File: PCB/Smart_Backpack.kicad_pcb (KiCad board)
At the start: 2 copper layers, 65.8 x 74.4 mm, 57 parts, among them J1 Conn_01x03_Pin, J2 Conn_01x02_Pin, J3 Conn_01x02_Pin, J4 Conn_01x03_Pin, J5 Conn_01x03_Pin, J6 Conn_01x03_Pin, J7 Conn_01x07_Pin, J8 Conn_01x08_Socket, J9 USB_C_Receptacle_USB2.0_16P, SW1 SW_Push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

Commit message: PCB revision 1 is finished!!!!
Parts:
- moved D2 4.09 mm to (93.2, 84.8), turned to 90 degrees
- moved R20 2.39 mm to (95.5, 85.6)
- moved R12 2.09 mm to (97.8, 87.4)
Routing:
- net +3V3: track 39.9 -> 241.8 mm, vias 1 -> 5
- net GND: track 0.00 -> 48.8 mm, vias 0 -> 7
- net Net-(C9-Pad1): track 5.62 -> 12.1 mm
- net Net-(C11-Pad1): track 4.91 -> 10.7 mm
- net unconnected-(U3-IO4-Pad24): track 0.00 -> 2.45 mm, vias 0 -> 1
- net Net-(J9-CC1): track 5.25 -> 7.40 mm
- net unconnected-(U3-IO19-Pad33): track 0.00 -> 2.09 mm, vias 0 -> 1
- net unconnected-(U3-IO21-Pad35): track 0.00 -> 2.04 mm, vias 0 -> 1
- net unconnected-(U3-IO5-Pad29): track 0.00 -> 1.78 mm, vias 0 -> 1
- net Flash_TXD: track 37.9 -> 39.5 mm, vias 0 -> 1
- net IMU_SDA: track 42.4 -> 41.0 mm
- net Flash_RXD: track 37.3 -> 38.6 mm, vias 0 -> 1
- net Net-(D2-A): track 3.28 -> 2.32 mm
- net FLEX_1: track 64.7 -> 64.6 mm, vias 0 -> 1
- added copper zone on B.Cu, net GND
- added copper zone on F.Cu, net GND
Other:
- outline, holes or cut-outs redrawn
- board text added: "Flash RX"
- board text added: "FlashTX"
- board text added: "IO19"
- board text added: "IO21"
- board text added: "IO4"
- board text added: "IO5"

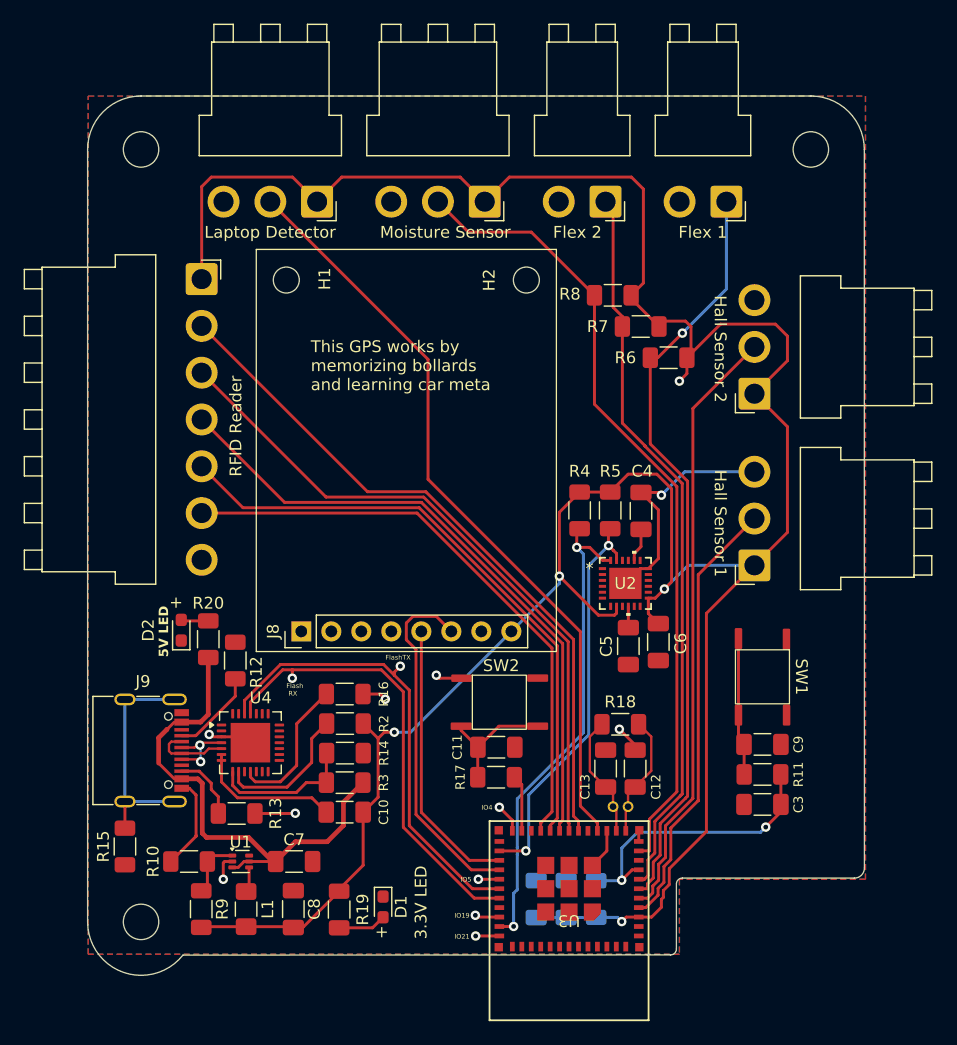
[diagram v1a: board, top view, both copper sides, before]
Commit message: add ground vias, RTC protection, and mounting hole exclusion zones
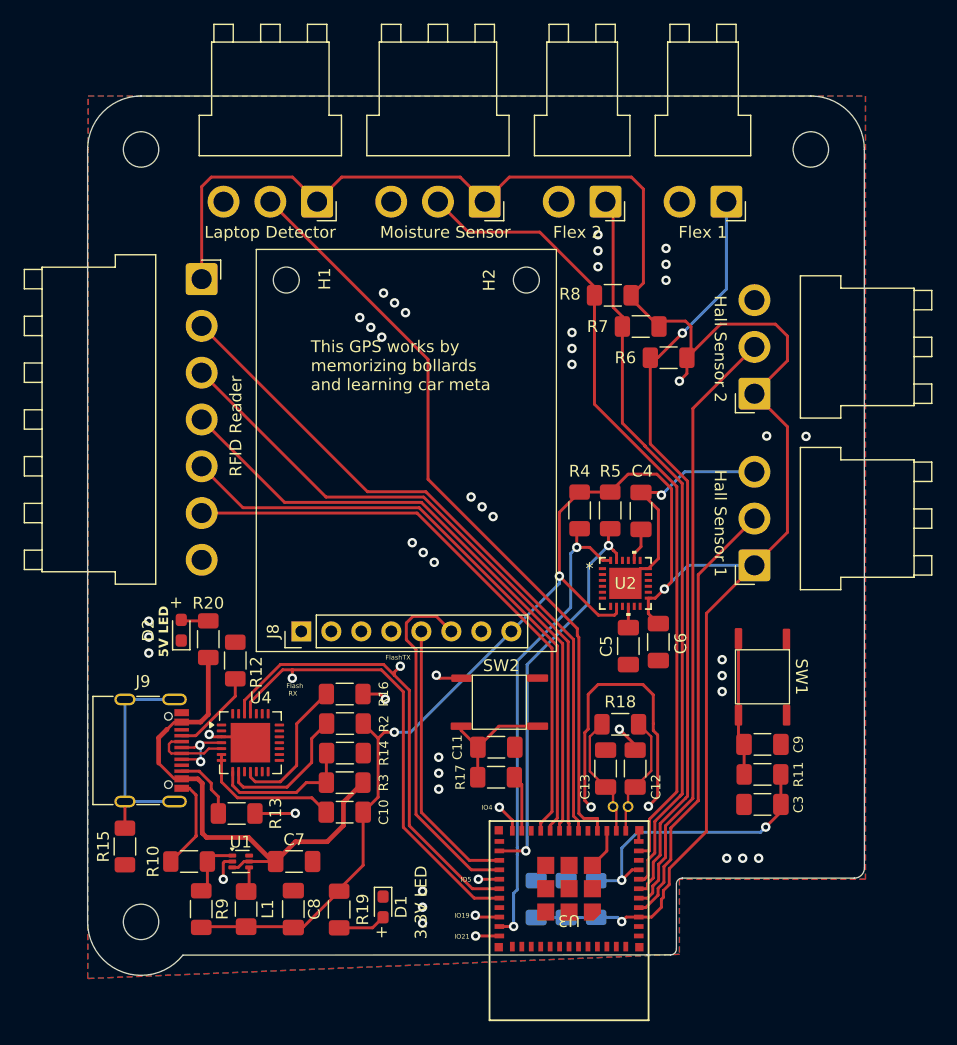
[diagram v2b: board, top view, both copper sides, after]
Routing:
- net GND: track 48.8 -> 74.9 mm, vias 7 -> 47
- net LAPTOP: track 64.7 -> 65.4 mm

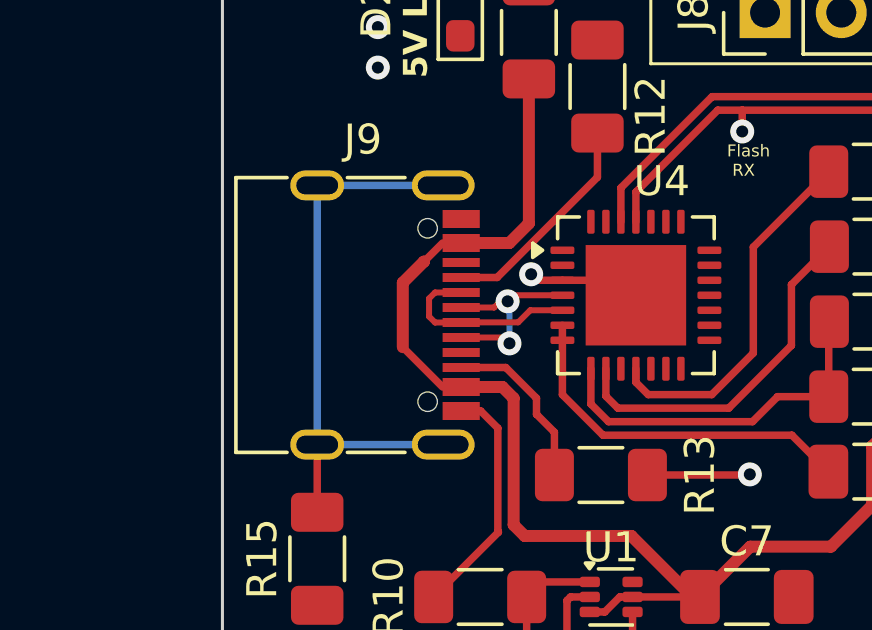
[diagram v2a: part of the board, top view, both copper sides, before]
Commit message: Some updates suggested by Ryan (The 1 sem senior design prof)
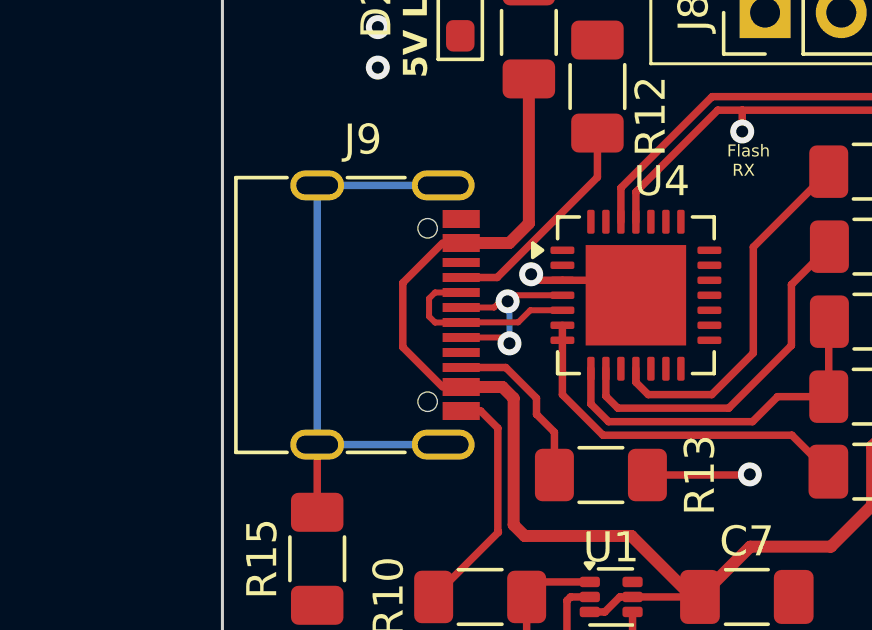
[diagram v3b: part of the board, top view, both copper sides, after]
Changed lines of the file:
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@@
-	)
-	(segment
-		(start 91.302 96.09)
-		(end 91.302 93.94)
-		(width 0.4)
-		(layer "F.Cu")
-		(net 21)
 	)
 	(segment
 		(start 100.954 104.415)
 		(end 98.922 102.383)
-		(width 0.4)
-		(layer "F.Cu")
-		(net 21)
-	)
-	(segment
-		(start 92.005 93.237)
-		(end 92.010364 93.237)
 		(width 0.4)
 		(layer "F.Cu")
@@
 	)
 	(segment
-		(start 92.629 97.417)
-		(end 91.302 96.09)
-		(width 0.25)
-		(layer "F.Cu")
-		(net 21)
-	)
-	(segment
 		(start 94.853124 92.617)
 		(end 95.504 91.966124)
@@
 	)
 	(segment
-		(start 91.302 93.94)
-		(end 92.005 93.237)
-		(width 0.4)
-		(layer "F.Cu")
-		(net 21)
-	)
-	(segment
 		(start 97.5355 104.915)
 		(end 98.035798 104.915)
-		(width 0.25)
-		(layer "F.Cu")
-		(net 21)
-	)
-	(segment
-		(start 92.010364 93.237)
-		(end 92.630364 92.617)
 		(width 0.25)
 		(layer "F.Cu")
@@
 	)
 	(segment
+		(start 92.630364 92.617)
+		(end 91.302 93.945364)
+		(width 0.25)
+		(layer "F.Cu")
+		(net 21)
+	)
+	(segment
 		(start 95.504 91.966124)
 		(end 95.504 87.148)
@@
 		(end 94.996 97.79)
 		(width 0.4)
+		(layer "F.Cu")
+		(net 21)
+	)
+	(segment
+		(start 91.302 93.945364)
+		(end 91.302 96.09)
+		(width 0.25)
 		(layer "F.Cu")
 		(net 21)
@@
 		(layer "F.Cu")
 		(net 21)
+	)
+	(segment
+		(start 91.302 96.09)
+		(end 92.629 97.417)
+		(width 0.25)
+		(layer "F.Cu")
+		(net 21)

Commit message: Literally just added our names
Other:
- board text added: "ECE49595 Team 10 Colin Fennen Grant Sylvester Josie Thomas Jack Douthit"
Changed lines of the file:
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@@
 		(layer "Edge.Cuts")
+	)
+	(gr_text "ECE49595\nTeam 10\nColin Fennen\nGrant Sylvester\nJosie Thomas\nJack Douthit"
+		(at 149.098 104.14 0)
+		(layer "B.Cu")
+		(effects
+			(font
+				(size 1.016 1.016)
+				(thickness 0.2286)
+				(bold yes)
+			)
+			(justify left bottom mirror)
+		)
 	)
 	(gr_text "+"

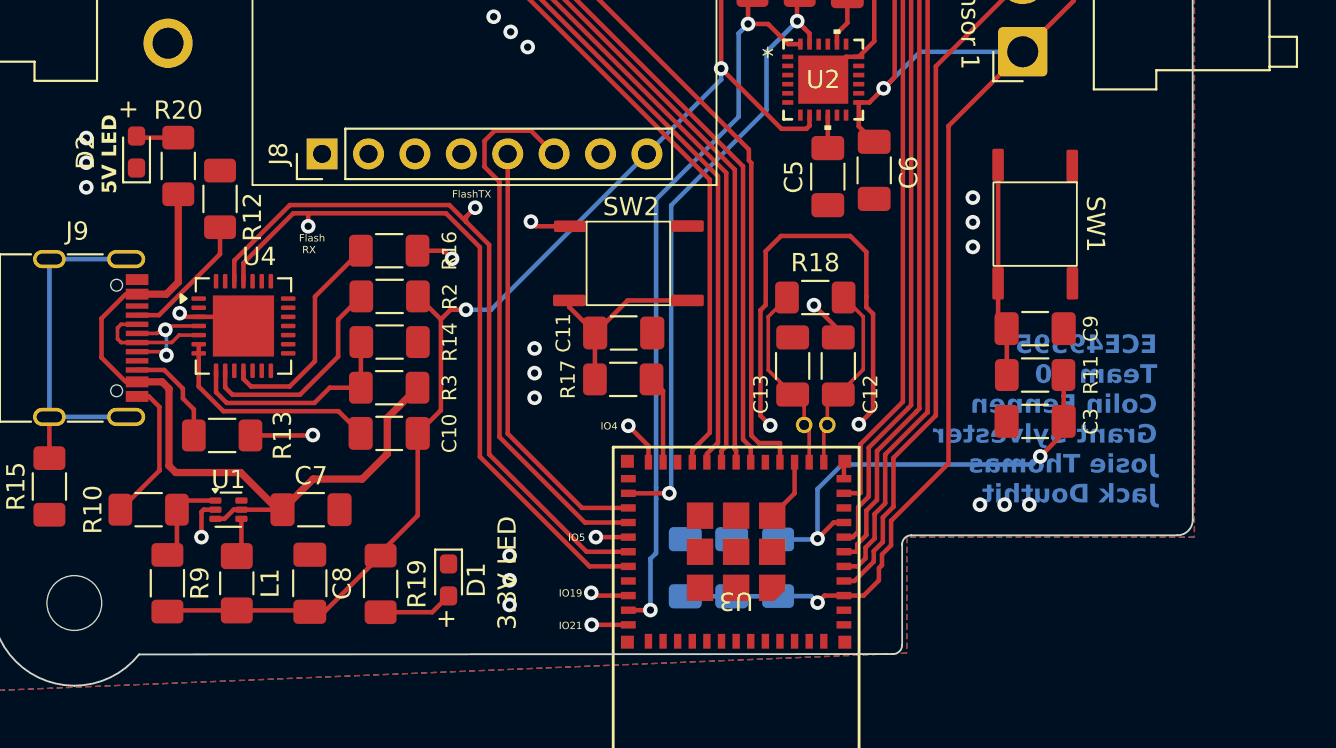
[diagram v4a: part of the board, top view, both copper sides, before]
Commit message: Added motors :pensive:
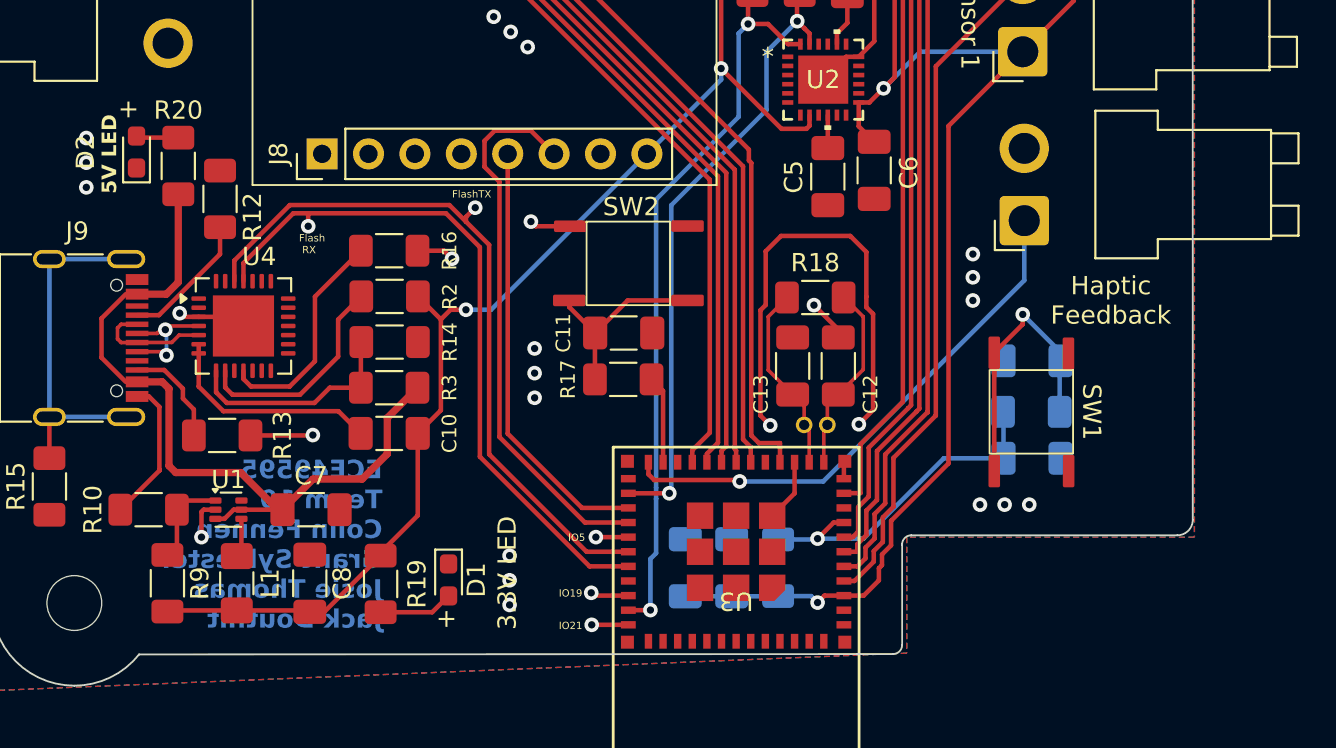
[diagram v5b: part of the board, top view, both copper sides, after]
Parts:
- added Haptic Feedback: Conn_01x02_Pin, Connector_JST:JST_VH_B2PS-VH_1x02_P3.96mm_Horizontal, F.Cu at (141.8, 88.6)
- C3, C9, R11: moved to B.Cu
- moved SW1 10.3 mm to (142.2, 99.1)
- moved R11 2.03 mm to (142.2, 99.1), turned to 180 degrees
- moved C3 2.02 mm to (142.2, 101.6), turned to 0 degrees
- moved C9 1.77 mm to (142.2, 96.3), turned to 180 degrees
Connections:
- U3 pad 24: unconnected-(U3-IO4-Pad24) -> MOTOR
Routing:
- net MOTOR: track 0.00 -> 29.0 mm, vias 0 -> 1
- net ESP_EN: track 24.7 -> 18.6 mm, vias 2 -> 1
- net Net-(C9-Pad1): track 12.1 -> 15.5 mm, vias 0 -> 1
- net unconnected-(U3-IO4-Pad24): track 2.45 -> 0.00 mm, vias 1 -> 0
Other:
- board text added: "Haptic Feedback"
- board text removed: "IO4"

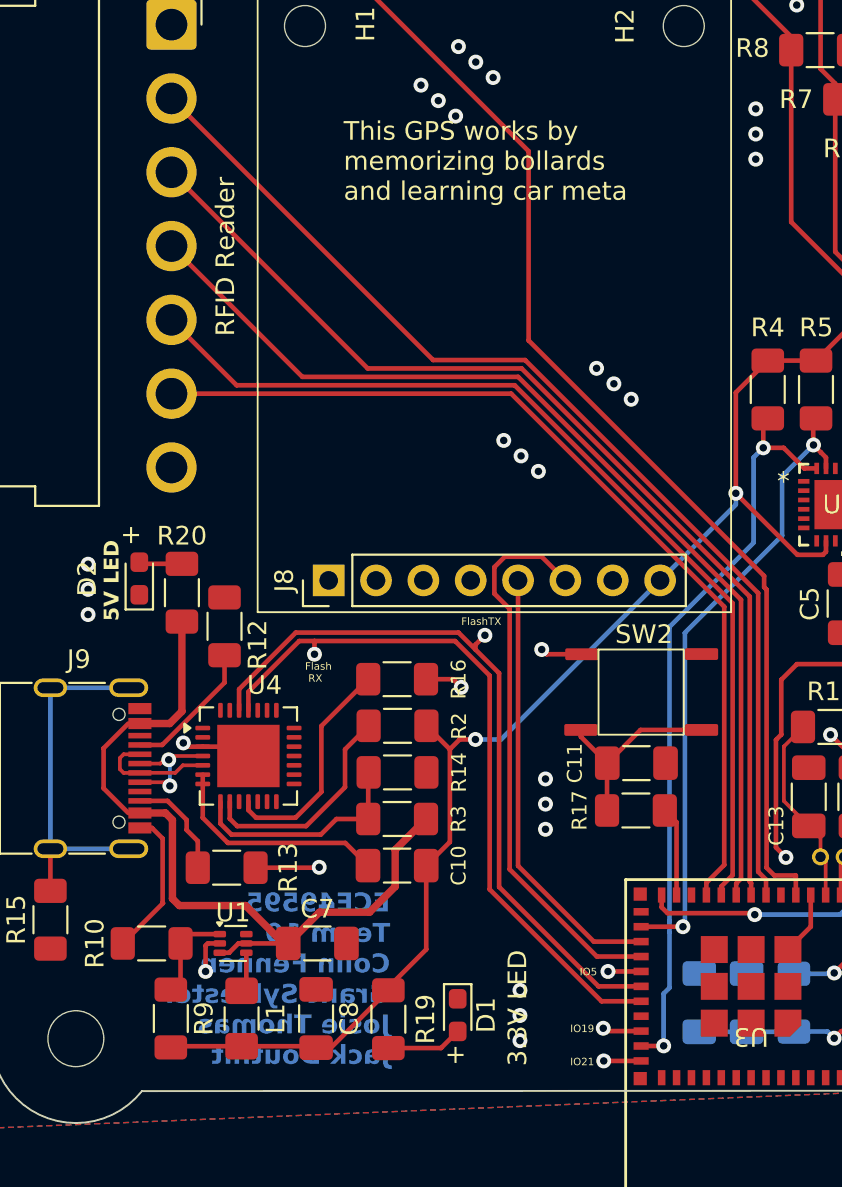
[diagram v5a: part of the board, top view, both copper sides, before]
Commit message: add datasheets to schematic and silkscreen board label
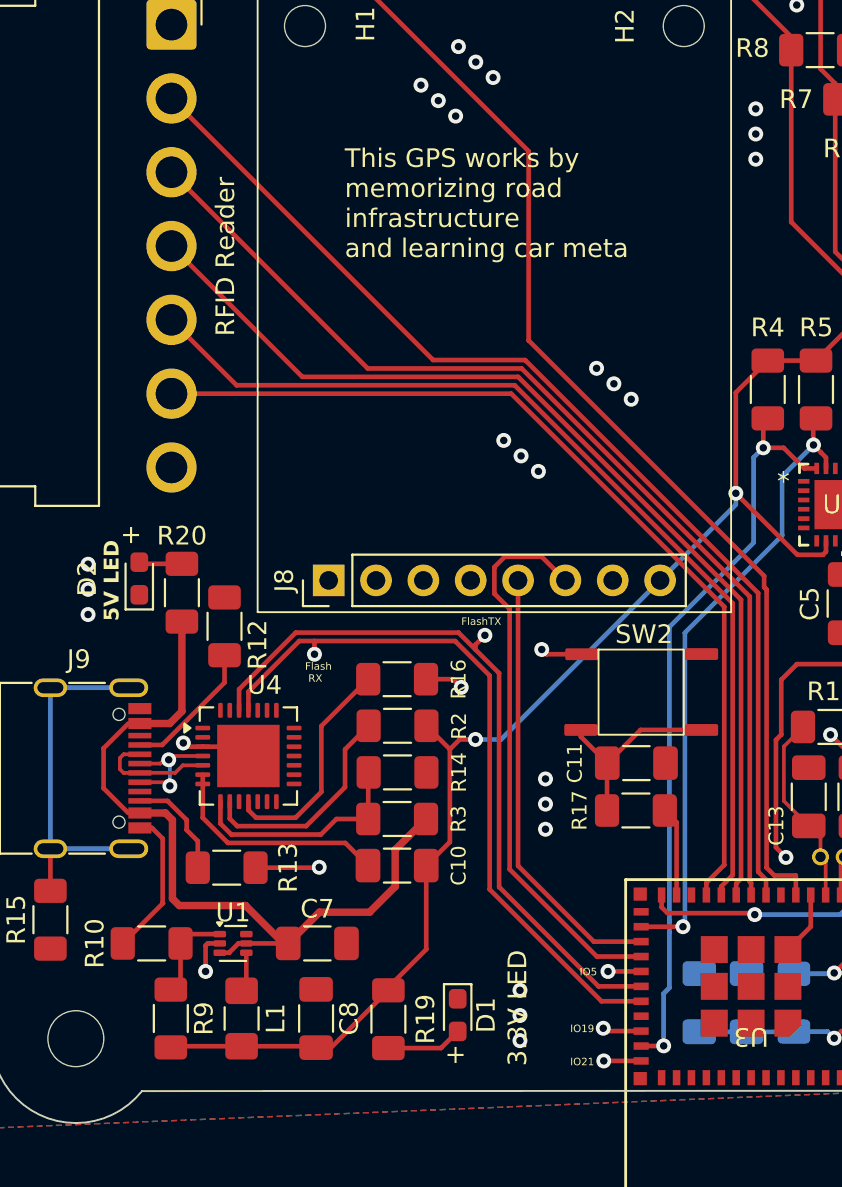
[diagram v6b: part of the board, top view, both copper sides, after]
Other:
- board text added: "Smart Backpack Main Board Rev. 1"
- board text added: "This GPS works by memorizing road infrastructure and learning car meta"
- board text removed: "This GPS works by memorizing bollards and learning car meta"
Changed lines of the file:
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@@
 		(layer "Edge.Cuts")
-	)
-	(gr_text "ECE49595\nTeam 10\nColin Fennen\nGrant Sylvester\nJosie Thomas\nJack Douthit"
-		(at 106.68 110.998 0)
-		(layer "B.Cu")
-		(effects
-			(font
-				(size 1.016 1.016)
-				(thickness 0.2286)
-				(bold yes)
-			)
-			(justify left bottom mirror)
-		)
 	)
 	(gr_text "+"
@@
 		)
 	)
-	(gr_text "This GPS works by\nmemorizing bollards\nand learning car meta"
-		(at 104.18 64.64 0)
+	(gr_text "This GPS works by\nmemorizing road \ninfrastructure\nand learning car meta"
+		(at 104.24 67.71 0)
 		(layer "F.SilkS")
 		(effects
@@
 		)
 	)
+	(gr_text "Smart Backpack\nMain Board\nRev. 1"
+		(at 124.17 68.92 0)
+		(layer "B.SilkS")
+		(effects
+			(font
+				(size 2 2)
+				(thickness 0.15)
+			)
+			(justify left bottom mirror)
+		)
+	)
+	(gr_text "ECE49595\nTeam 10\nColin Fennen\nGrant Sylvester\nJosie Thomas\nJack Douthit"
+		(at 107.65 111.12 0)
+		(layer "B.SilkS")
+		(effects
+			(font
+				(size 1.016 1.016)
+				(thickness 0.2286)
+				(bold yes)
+			)
+			(justify left bottom mirror)
+		)
+	)
